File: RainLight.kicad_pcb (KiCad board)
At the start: 2 copper layers, 120 x 55 mm, 25 parts, among them J1 DTM04-2P (wire pigtail)

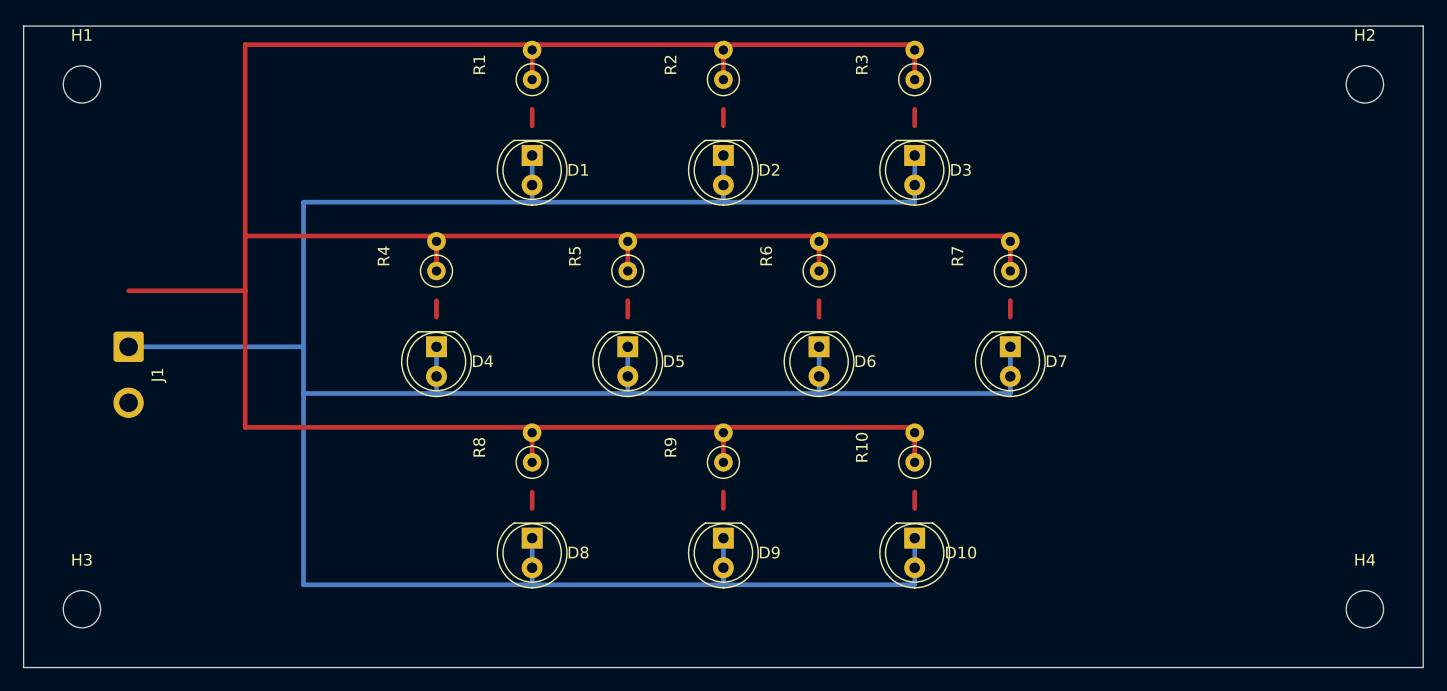
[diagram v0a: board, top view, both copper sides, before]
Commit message: Swap resistors to flat/horizontal 7.62mm footprint
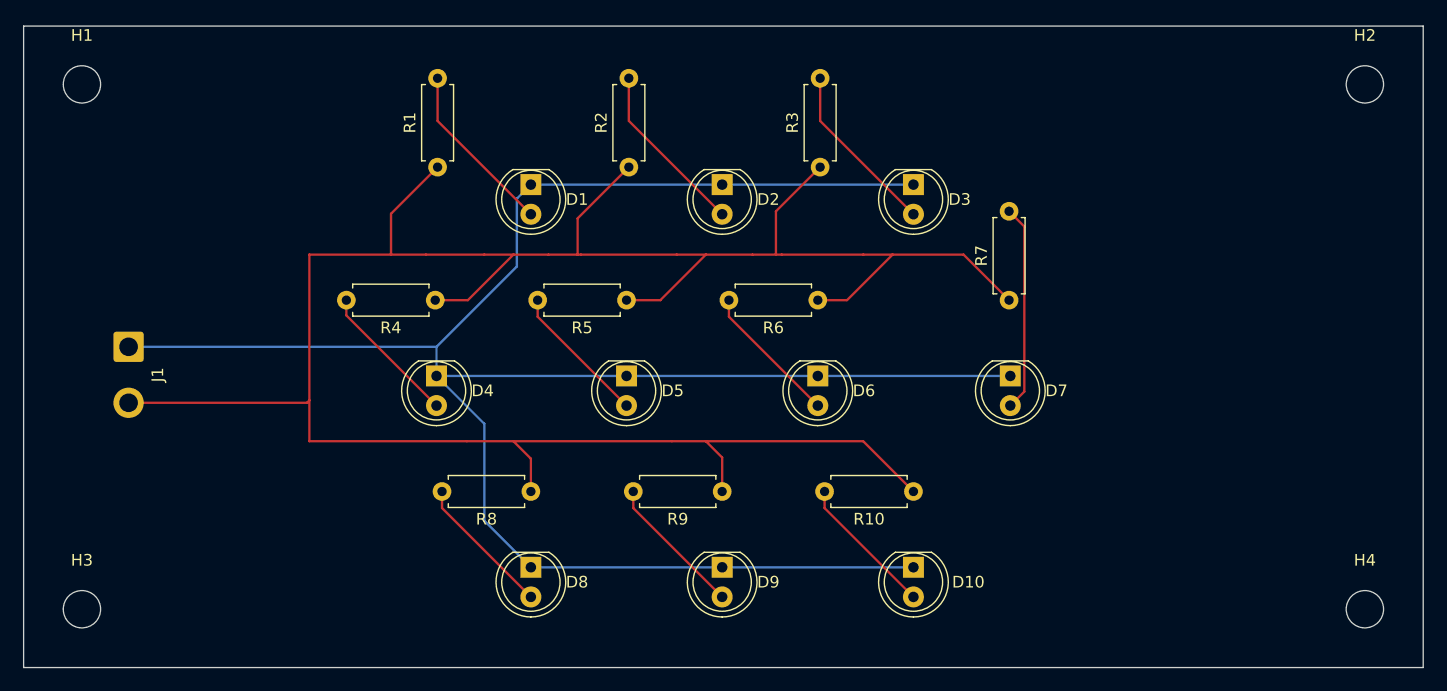
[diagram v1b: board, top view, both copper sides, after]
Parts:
- H1, H2, H3, H4: footprint MountingHole_3.2mm_M3 -> MountingHole:MountingHole_3.2mm_M3
- R1, R10, R2, R3, R4, R5, R6, R7, R8, R9: footprint Resistor_THT:R_Axial_DIN0207_L6.3mm_D2.5mm_P2.54mm_Vertical -> Resistor_THT:R_Axial_DIN0207_L6.3mm_D2.5mm_P7.62mm_Horizontal
- moved R1 11.0 mm to (116.5, 93.0)
- moved R2 11.0 mm to (132.9, 93.0)
- moved R3 11.0 mm to (149.3, 93.0)
- moved D1 2.50 mm to (124.5, 94.5)
- moved D5 2.50 mm to (132.7, 110.9)
- moved D8 2.50 mm to (124.5, 127.3)
- moved R5 2.50 mm to (132.7, 104.4), turned to 180 degrees
- moved R8 2.50 mm to (124.5, 120.8), turned to 180 degrees
- moved R4 2.50 mm to (116.3, 104.4), turned to 180 degrees
- moved D10 2.50 mm to (157.3, 127.3)
- moved D2 2.50 mm to (140.9, 94.5)
- moved D3 2.50 mm to (157.3, 94.5)
- moved D6 2.50 mm to (149.1, 110.9)
- moved D9 2.50 mm to (140.9, 127.3)
- moved R10 2.50 mm to (157.3, 120.8), turned to 180 degrees
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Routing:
- net GND: track 253.2 -> 180.7 mm
- net VCC: track 253.2 -> 208.9 mm
- net Net-(D7-A): track 1.42 -> 17.7 mm
- net Net-(D3-A): track 1.42 -> 15.0 mm
- net Net-(D2-A): track 1.42 -> 15.0 mm
- net Net-(D1-A): track 1.42 -> 15.0 mm
- net Net-(D4-A): track 1.42 -> 12.2 mm
- net Net-(D9-A): track 1.42 -> 12.2 mm
- net Net-(D6-A): track 1.42 -> 12.2 mm
- net Net-(D10-A): track 1.42 -> 12.2 mm
- net Net-(D8-A): track 1.42 -> 12.2 mm
- net Net-(D5-A): track 1.42 -> 12.2 mm

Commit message: Update R1-R10 from 1.2k to 510 ohm
Based on confirmed LED spec (Chanzon 10mm red, Vf=2.0V @ 20mA) at 12V
source: R = (12-2)/0.02 = 500 ohm, rounded to nearest standard value (510).
Value-only change - footprint/wattage unchanged, still the 1/4W-sized
DIN0207 axial package. Actual dissipation at 510ohm/20mA is ~0.2W, close
to the 1/4W package's rating - a genuine 1/2W part would need a larger
footprint (not yet done, pending a real part number).
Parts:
- R1, R10, R2, R3, R4, R5, R6, R7, R8, R9: value 1.2k -> 510
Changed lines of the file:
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@@
 			)
 		)
-		(property "Value" "1.2k"
+		(property "Value" "510"
 			(at 3.81 2.37 90)
 			(layer "F.Fab")
@@
 			)
 		)
-		(property "Value" "1.2k"
+		(property "Value" "510"
 			(at 3.81 2.37 90)
 			(layer "F.Fab")
@@
 			)
 		)
-		(property "Value" "1.2k"
+		(property "Value" "510"
 			(at 3.81 2.37 90)
 			(layer "F.Fab")
@@
 			)
 		)
-		(property "Value" "1.2k"
+		(property "Value" "510"
 			(at 3.81 2.37 0)
 			(layer "F.Fab")
@@
 			)
 		)
-		(property "Value" "1.2k"
+		(property "Value" "510"
 			(at 3.81 2.37 0)
 			(layer "F.Fab")
@@
 			)
 		)
-		(property "Value" "1.2k"
+		(property "Value" "510"
 			(at 3.81 2.37 90)
 			(layer "F.Fab")
@@
 			)
 		)
-		(property "Value" "1.2k"
+		(property "Value" "510"
 			(at 3.81 2.37 0)
 			(layer "F.Fab")
@@
 			)
 		)
-		(property "Value" "1.2k"
+		(property "Value" "510"
 			(at 3.81 2.37 0)
 			(layer "F.Fab")
@@
 			)
 		)
-		(property "Value" "1.2k"
+		(property "Value" "510"
 			(at 3.81 2.37 0)
 			(layer "F.Fab")
@@
 			)
 		)
-		(property "Value" "1.2k"
+		(property "Value" "510"
 			(at 3.81 2.37 0)
 			(layer "F.Fab")
